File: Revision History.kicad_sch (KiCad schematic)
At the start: 0 parts

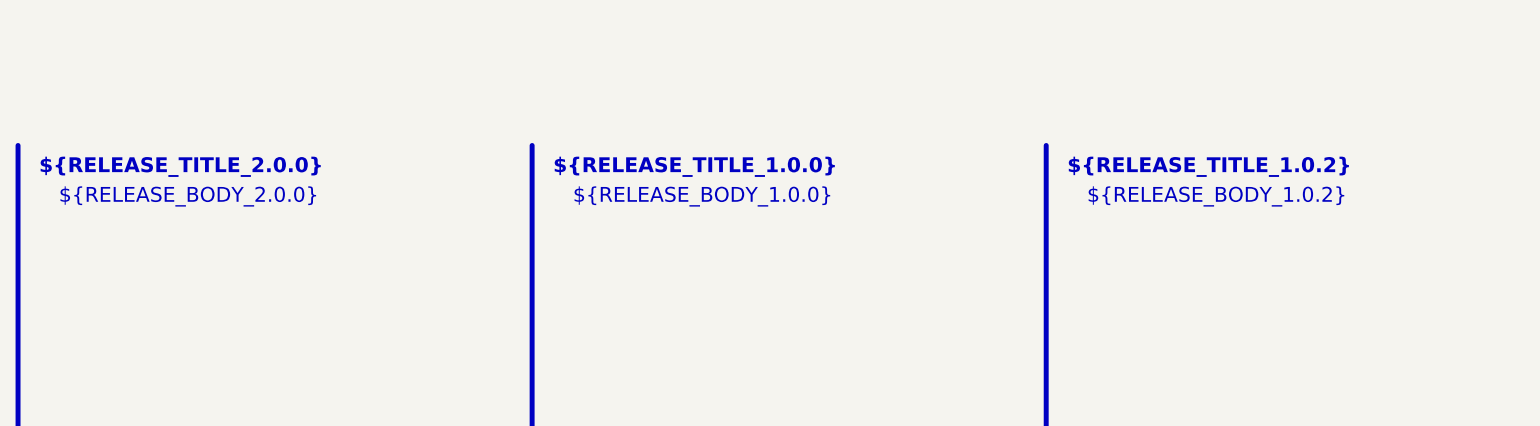
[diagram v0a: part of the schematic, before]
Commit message: Updated C22 and C23
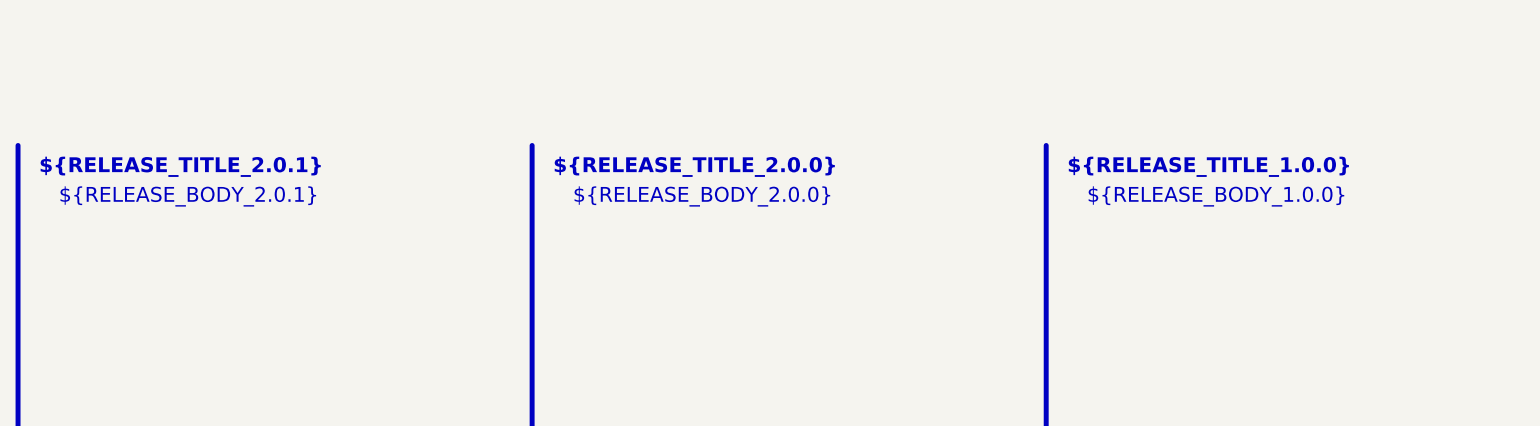
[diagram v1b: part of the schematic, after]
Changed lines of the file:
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@@
 		)
 	)
-	(text_box "${RELEASE_BODY_2.0.0}"
+	(text_box "${RELEASE_BODY_2.0.1}"
 		(exclude_from_sim no)
 		(at 22.86 35.56 0)
@@
 		)
 	)
-	(text_box "${RELEASE_TITLE_1.0.2}"
+	(text_box "${RELEASE_TITLE_1.0.0}"
 		(exclude_from_sim no)
 		(at 152.4 31.75 0)
@@
 		)
 	)
-	(text_box "${RELEASE_BODY_1.0.2}"
+	(text_box "${RELEASE_BODY_1.0.0}"
 		(exclude_from_sim no)
 		(at 154.94 35.56 0)
@@
 		)
 	)
-	(text_box "${RELEASE_BODY_1.0.0}"
+	(text_box "${RELEASE_BODY_2.0.0}"
 		(exclude_from_sim no)
 		(at 88.9 35.56 0)
@@
 		)
 	)
-	(text_box "${RELEASE_TITLE_2.0.0}"
+	(text_box "${RELEASE_TITLE_2.0.1}"
 		(exclude_from_sim no)
 		(at 20.32 31.75 0)
@@
 		)
 	)
-	(text_box "${RELEASE_TITLE_1.0.0}"
+	(text_box "${RELEASE_TITLE_2.0.0}"
 		(exclude_from_sim no)
 		(at 86.36 31.75 0)
